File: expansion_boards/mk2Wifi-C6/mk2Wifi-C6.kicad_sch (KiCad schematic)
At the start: 28 parts, among them J0 TRIG_EXT, J2 USB_C_Receptacle_USB2.0_16P, J3 UART_EXT, J4 OLED, SW1 SW_Push, U1 ESP32-C3-MINI-1, U2 AP2112K-3.3

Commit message: Migrate mk2Wifi-C6 schematic to ESP32-C6-MINI-1
- Replace ESP32-C3-MINI-1 with ESP32-C6-MINI-1 (PCM_Espressif symbol)
- Reassign LED GPIOs to left-side pins: D5→IO4, D6→IO5, D7→IO3, D8→IO0, D9→IO1
- Move DS18B20 to right-side IO23 for direct routing to J3
- USB on IO12/IO13, I2C on IO6/IO7, UART unchanged
- Remove local PCM_Espressif footprint library (use global)
- Remove C3 footprint file from C6 project

Co-Authored-By: Claude Opus 4.6 <noreply@anthropic.com>
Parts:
- removed R4: 10K, Resistor_SMD:R_0402_1005Metric, symbol Device:R
- removed U1: ESP32-C3-MINI-1, PCM_Espressif:ESP32-C3-MINI-1, symbol PCM_Espressif:ESP32-C3-MINI-1
- added U1: ESP32-C6-MINI-1/U, PCM_Espressif:ESP32-C6-MINI-1, symbol PCM_Espressif:ESP32-C6-MINI-1/U
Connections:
- net +3V3: now also U1.3 (3V3)
- net DS18B20: now also U1.29 (GPIO23)
- net GND: now also U1.1 (GND), U1.11 (GND), U1.14 (GND), U1.2 (GND), U1.36 (GND), U1.37 (GND), U1.38 (GND), U1.39 (GND), U1.40 (GND), U1.41 (GND), U1.42 (GND), U1.43 (GND), U1.44 (GND), U1.45 (GND), U1.46 (GND), U1.47 (GND), U1.48 (GND), U1.49 (GND), U1.50 (GND), U1.51 (GND), U1.52 (GND), U1.53 (GND)
- net GPIO8: now also U1.22 (GPIO8)
- net GPIO9: now also U1.23 (GPIO9)
- net SCL: now also U1.16 (MTDO/GPIO7)
- net SDA: now also U1.15 (MTCK/GPIO6/ADC1_CH6)
- net UART_RX: now also U1.31 (U0TXD/GPIO16)
- net UART_TX: now also U1.30 (U0RXD/GPIO17)
- net USB_DN: now also U1.17 (GPIO12/USB_D-)
- net USB_DP: now also U1.18 (GPIO13/USB_D+)
- net at R7.1: now also U1.6 (GPIO3/ADC1_CH3)
- net at R5.2: now also U1.9 (MTMS/GPIO4/ADC1_CH4)
- net at C4.1, R1.2: now also U1.8 (EN/CHIP_PU)
- net at R8.1: now also U1.12 (GPIO0/ADC1_CH0/XTAL_32K_P)
- net at R6.1: now also U1.10 (MTDI/GPIO5/ADC1_CH5)
- net at R9.2: now also U1.13 (GPIO1/ADC1_CH1/XTAL_32K_N)
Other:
- moved on the sheet: J2, R10, R11, R5, R6, R7, R9

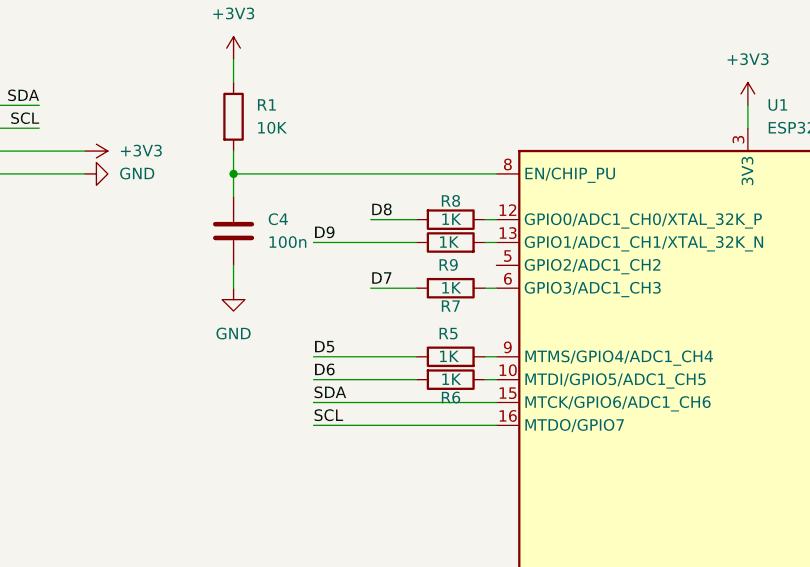
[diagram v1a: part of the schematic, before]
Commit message: Update mk2Wifi-C6 PCB layout, routing, and LCSC refs
- Complete PCB routing for ESP32-C6-MINI-1 board
- Add GND copper pours on F.Cu and B.Cu with 51 stitching vias
- Add +5V pour on F.Cu
- Add USB diff pair, I2C, UART, GPIO signal routing
- Add LCSC part number C5736265 for U1 (ESP32-C6-MINI-1-N4)
- Update project settings (USB net class, track widths)

Co-Authored-By: Claude Opus 4.6 <noreply@anthropic.com>
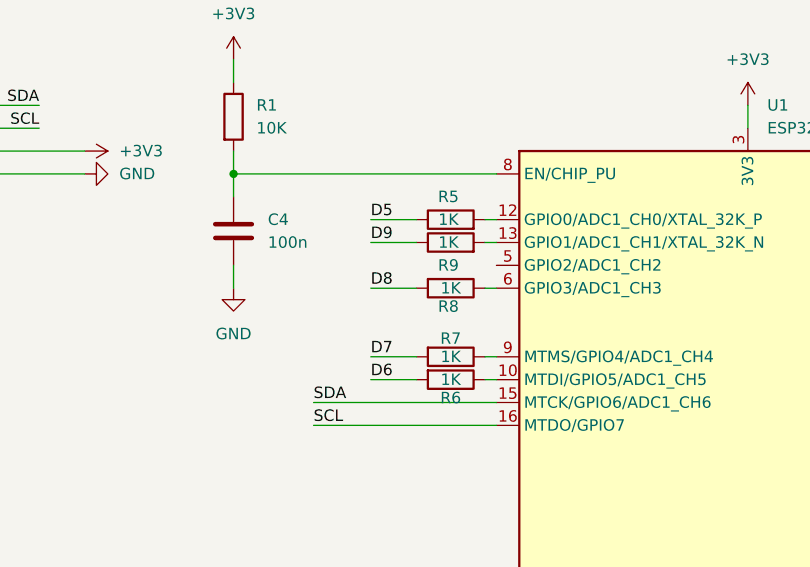
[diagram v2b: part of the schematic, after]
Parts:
- U1: LCSC (none) -> C5736265
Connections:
- net at R7.1: now also U1.9 (MTMS/GPIO4/ADC1_CH4); no longer U1.6 (GPIO3/ADC1_CH3)
- net at R5.2: now also U1.12 (GPIO0/ADC1_CH0/XTAL_32K_P); no longer U1.9 (MTMS/GPIO4/ADC1_CH4)
- net at R8.1: now also U1.6 (GPIO3/ADC1_CH3); no longer U1.12 (GPIO0/ADC1_CH0/XTAL_32K_P)
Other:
- moved on the sheet: R5, R7, R8
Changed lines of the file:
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@@
 	(wire
 		(pts
-			(xy 156.21 46.99) (xy 151.13 46.99)
-		)
-		(stroke
-			(width 0)
-			(type default)
-		)
-	)
-	(wire
-		(pts
 			(xy 68.58 177.8) (xy 68.58 180.34)
 		)
@@
 	(wire
 		(pts
-			(xy 135.89 21.59) (xy 135.89 24.13)
+			(xy 156.21 54.61) (xy 151.13 54.61)
 		)
 		(stroke
@@
 	(wire
 		(pts
-			(xy 91.44 55.88) (xy 91.44 58.42)
+			(xy 135.89 21.59) (xy 135.89 24.13)
 		)
 		(stroke
@@
 	(wire
 		(pts
-			(xy 220.98 57.15) (xy 241.3 57.15)
+			(xy 91.44 55.88) (xy 91.44 58.42)
 		)
 		(stroke
@@
 	(wire
 		(pts
-			(xy 165.1 62.23) (xy 144.78 62.23)
+			(xy 220.98 57.15) (xy 241.3 57.15)
 		)
 		(stroke
@@
 	(wire
 		(pts
-			(xy 163.83 39.37) (xy 165.1 39.37)
+			(xy 165.1 62.23) (xy 144.78 62.23)
 		)
 		(stroke
@@
 	(wire
 		(pts
-			(xy 156.21 57.15) (xy 144.78 57.15)
+			(xy 156.21 57.15) (xy 151.13 57.15)
 		)
 		(stroke
@@
 	(wire
 		(pts
-			(xy 144.78 41.91) (xy 156.21 41.91)
+			(xy 151.13 41.91) (xy 156.21 41.91)
 		)
 		(stroke
@@
 	(wire
 		(pts
-			(xy 156.21 39.37) (xy 151.13 39.37)
+			(xy 49.53 158.75) (xy 52.07 158.75)
 		)
 		(stroke
@@
 	(wire
 		(pts
-			(xy 49.53 158.75) (xy 52.07 158.75)
+			(xy 165.1 39.37) (xy 163.83 39.37)
 		)
 		(stroke
@@
 	(wire
 		(pts
+			(xy 163.83 54.61) (xy 165.1 54.61)
+		)
+		(stroke
+			(width 0)
+			(type default)
+		)
+	)
+	(wire
+		(pts
 			(xy 220.98 41.91) (xy 241.3 41.91)
 		)
@@
 	(wire
 		(pts
-			(xy 165.1 54.61) (xy 163.83 54.61)
+			(xy 156.21 46.99) (xy 151.13 46.99)
 		)
 		(stroke
@@
 	(wire
 		(pts
-			(xy 144.78 54.61) (xy 156.21 54.61)
+			(xy 191.77 97.79) (xy 193.04 97.79)
 		)
 		(stroke
@@
 	(wire
 		(pts
-			(xy 191.77 97.79) (xy 193.04 97.79)
+			(xy 52.07 156.21) (xy 78.74 156.21)
 		)
 		(stroke
@@
 	(wire
 		(pts
-			(xy 52.07 156.21) (xy 78.74 156.21)
+			(xy 52.07 163.83) (xy 49.53 163.83)
 		)
 		(stroke
@@
 	(wire
 		(pts
-			(xy 52.07 163.83) (xy 49.53 163.83)
+			(xy 27.94 33.02) (xy 36.83 33.02)
 		)
 		(stroke
@@
 	(wire
 		(pts
-			(xy 27.94 33.02) (xy 36.83 33.02)
+			(xy 53.34 35.56) (xy 64.77 35.56)
 		)
 		(stroke
@@
 	(wire
 		(pts
-			(xy 53.34 35.56) (xy 64.77 35.56)
+			(xy 55.88 113.03) (xy 55.88 115.57)
 		)
 		(stroke
@@
 	(wire
 		(pts
-			(xy 55.88 113.03) (xy 55.88 115.57)
+			(xy 151.13 39.37) (xy 156.21 39.37)
 		)
 		(stroke
@@
 	)
 	(label "D5"
-		(at 144.78 54.61 0)
+		(at 151.13 39.37 0)
 		(effects
 			(font
@@
 		)
 	)
-	(label "D8"
-		(at 151.13 39.37 0)
-		(effects
-			(font
-				(size 1.27 1.27)
-			)
-			(justify left bottom)
-		)
-	)
 	(label "D9"
-		(at 144.78 41.91 0)
+		(at 151.13 41.91 0)
 		(effects
 			(font
@@
 		)
 	)
-	(label "D7"
-		(at 151.13 46.99 0)
-		(effects
-			(font
-				(size 1.27 1.27)
-			)
-			(justify left bottom)
-		)
-	)
 	(label "DS18B20"
 		(at 241.3 77.47 180)
@@
 		)
 	)
+	(label "D7"
+		(at 151.13 54.61 0)
+		(effects
+			(font
+				(size 1.27 1.27)
+			)
+			(justify left bottom)
+		)
+	)
 	(label "D6"
 		(at 53.34 33.02 0)
@@
 	)
 	(label "D6"
-		(at 144.78 57.15 0)
+		(at 151.13 57.15 0)
 		(effects
 			(font
@@
 		)
 	)
+	(label "D8"
+		(at 151.13 46.99 0)
+		(effects
+			(font
+				(size 1.27 1.27)
+			)
+			(justify left bottom)
+		)
+	)
 	(symbol
 		(lib_id "Device:R")
-		(at 160.02 46.99 270)
+		(at 160.02 54.61 270)
 		(unit 1)
 		(exclude_from_sim no)
@@
 		(dnp no)
 		(property "Reference" "R7"
-			(at 160.02 49.022 90)
+			(at 160.02 52.578 90)
 			(effects
 				(font
@@
 		)
 		(property "Value" "1K"
-			(at 160.02 46.99 90)
+			(at 160.02 54.61 90)
 			(effects
 				(font
@@
 		)
 		(property "Footprint" "Resistor_SMD:R_0402_1005Metric"
-			(at 160.02 45.212 90)
+			(at 160.02 52.832 90)
 			(effects
 				(font
@@
 		)
 		(property "Datasheet" "~"
-			(at 160.02 46.99 0)
+			(at 160.02 54.61 0)
 			(effects
 				(font
@@
 		)
 		(property "Description" "Resistor"
-			(at 160.02 46.99 0)
+			(at 160.02 54.61 0)
 			(effects
 				(font
@@
 		)
 		(property "LCSC" "C11702"
-			(at 160.02 46.99 0)
+			(at 160.02 54.61 0)
 			(effects
 				(font
@@
 	(symbol
 		(lib_id "Device:R")
-		(at 160.02 54.61 90)
+		(at 160.02 39.37 90)
 		(unit 1)
 		(exclude_from_sim no)
@@
 		(dnp no)
 		(property "Reference" "R5"
-			(at 159.766 52.07 90)
+			(at 159.766 36.83 90)
 			(effects
 				(font
@@
 		)
 		(property "Value" "1K"
-			(at 159.766 54.61 90)
+			(at 159.766 39.37 90)
 			(effects
 				(font
@@
 		)
 		(property "Footprint" "Resistor_SMD:R_0402_1005Metric"
-			(at 160.02 56.388 90)
+			(at 160.02 41.148 90)
 			(effects
 				(font
@@
 		)
 		(property "Datasheet" "~"
-			(at 160.02 54.61 0)
+			(at 160.02 39.37 0)
 			(effects
 				(font
@@
 		)
 		(property "Description" "Resistor"
-			(at 160.02 54.61 0)
+			(at 160.02 39.37 0)
 			(effects
 				(font
@@
 		)
 		(property "LCSC" "C11702"
-			(at 159.766 54.61 0)
+			(at 159.766 39.37 0)
 			(effects
 				(font
@@
 			)
 		)
+		(property "LCSC" "C5736265"
+			(at 193.04 62.23 0)
+			(effects
+				(font
+					(size 1.27 1.27)
+				)
+				(hide yes)
+			)
+		)
 		(pin "15"
 		)
@@
 	(symbol
 		(lib_id "Device:R")
-		(at 160.02 39.37 270)
+		(at 160.02 46.99 270)
 		(unit 1)
 		(exclude_from_sim no)
@@
 		(dnp no)
 		(property "Reference" "R8"
-			(at 160.02 37.338 90)
+			(at 159.766 49.022 90)
 			(effects
 				(font
@@
 		)
 		(property "Value" "1K"
-			(at 160.02 39.37 90)
+			(at 160.02 46.99 90)
 			(effects
 				(font
@@
 		)
 		(property "Footprint" "Resistor_SMD:R_0402_1005Metric"
-			(at 160.02 37.592 90)
+			(at 160.02 45.212 90)
 			(effects
 				(font
@@
 		)
 		(property "Datasheet" "~"
-			(at 160.02 39.37 0)
+			(at 160.02 46.99 0)
 			(effects
 				(font
@@
 		)
 		(property "Description" "Resistor"
-			(at 160.02 39.37 0)
+			(at 160.02 46.99 0)
 			(effects
 				(font
@@
 		)
 		(property "LCSC" "C11702"
-			(at 160.02 39.37 0)
+			(at 160.02 46.99 0)
 			(effects
 				(font

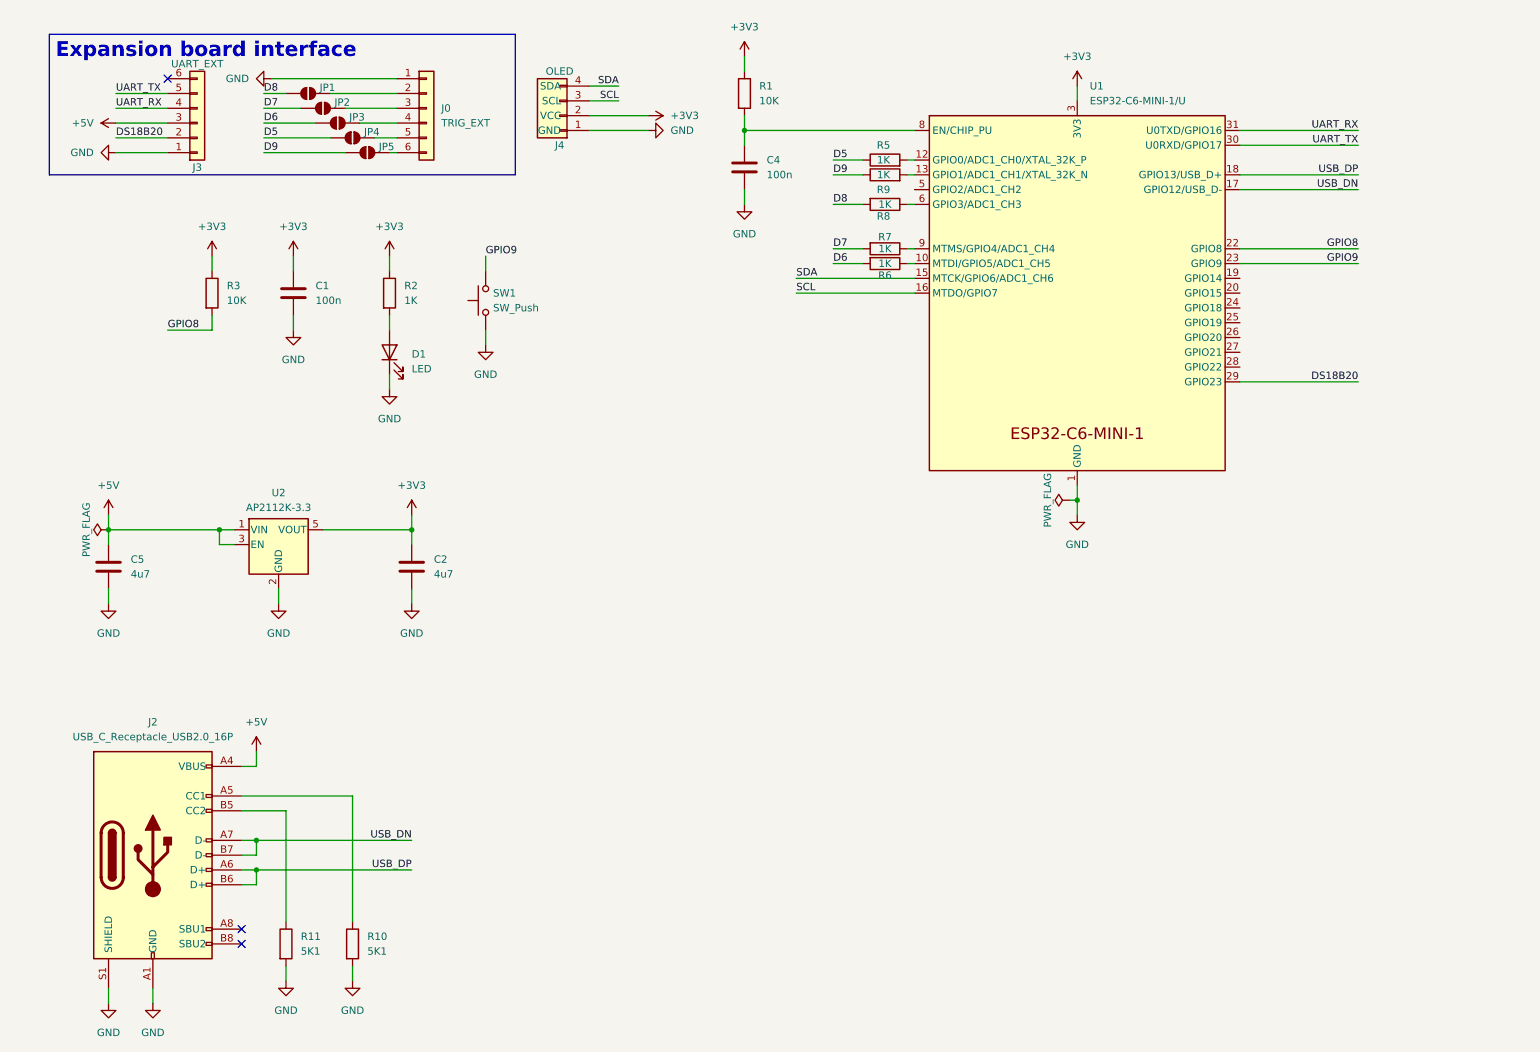
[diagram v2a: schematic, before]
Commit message: Add schematic descriptions and SVG exports to mk2Wifi READMEs
- Add title block comments (description, MCU, power, license) to both C3 and C6 schematics
- Rename C3 schematic title from "mk2Wifi" to "mk2Wifi-C3"
- Export schematic SVGs and add Schematic sections to all four READMEs

Co-Authored-By: Claude Opus 4.6 <noreply@anthropic.com>
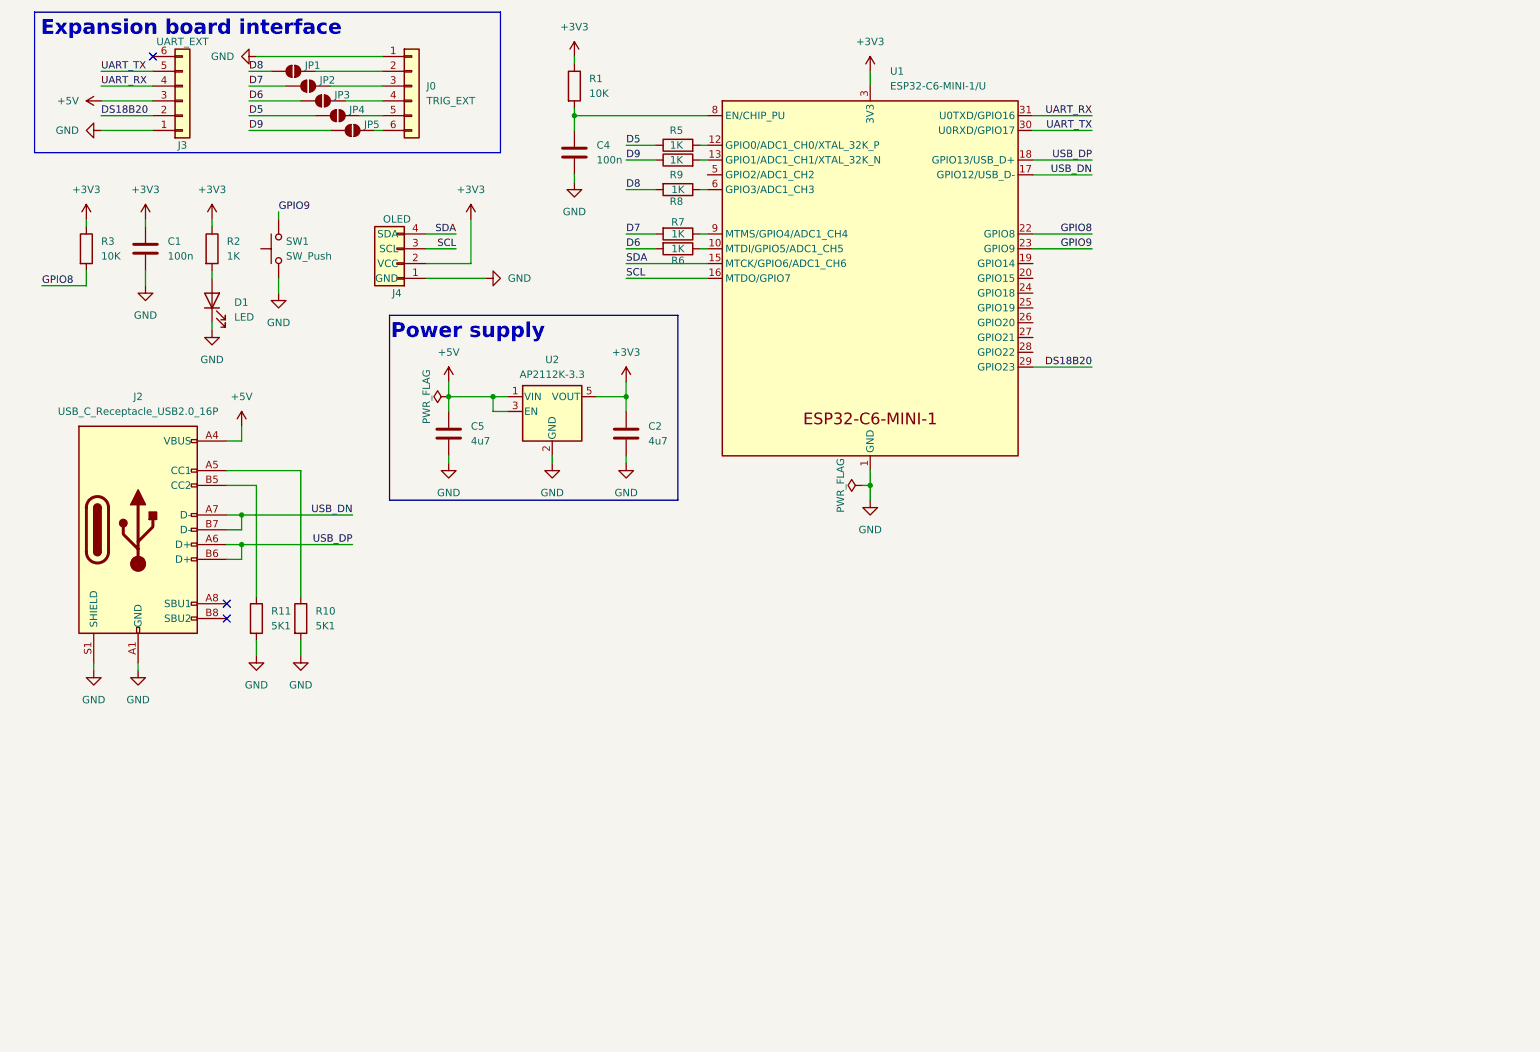
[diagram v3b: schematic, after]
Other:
- note added: "Power supply"
- moved on the sheet: C1, C2, C4, C5, D1, J0, J2, J3, J4, JP1, JP2, JP3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

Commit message: Add MISC GPIO connector and update mk2Wifi-C6 docs
Add 5-pin MISC header (GPIO19-22) for additional user I/O.
Update readmes with complete strapping pin documentation (all 5 pins),
corrected UART GPIO mapping (GPIO16/GPIO17), new connector pinouts,
and regenerated schematic PDF/SVG. Rename UART_EXT connector to J0.

Co-Authored-By: Claude Opus 4.6 <noreply@anthropic.com>
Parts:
- added J4: MISC, Connector_PinHeader_2.54mm:PinHeader_1x05_P2.54mm_Vertical, symbol Connector_Generic:Conn_01x05
- SW1: value SW_Push -> Boot
- renumbered J3 to J0, J0 to J1, J4 to J3
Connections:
- net GND: now also J4.1 (Pin_1)
- net GPIO19: now reaches U1.25 (GPIO19)
- net GPIO19: now also J4.2 (Pin_2)
- net GPIO20: now reaches U1.26 (GPIO20)
- net GPIO20: now also J4.3 (Pin_3)
- net GPIO21: now reaches U1.27 (GPIO21)
- net GPIO21: now also J4.4 (Pin_4)
- net GPIO22: now reaches U1.28 (GPIO22)
- net GPIO22: now also J4.5 (Pin_5)
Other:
- moved on the sheet: C1, D1, R2, R3, SW1
